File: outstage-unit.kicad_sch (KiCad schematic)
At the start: 10 parts, among them J2101 Conn_01x06_Socket, M2101 Fan

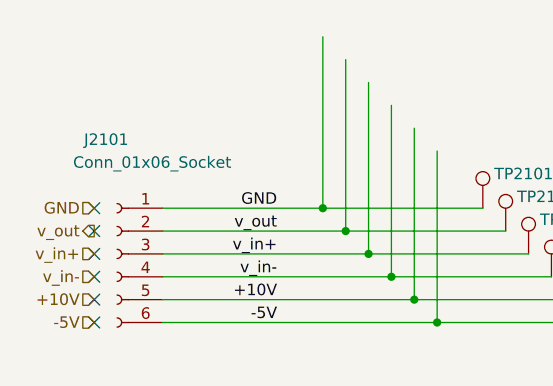
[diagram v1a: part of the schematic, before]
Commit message: edit outstage connector pin out for outstage-unit
enhance layout option with other pin out and mirror pinout for second outstage.
This allows to create a better layout with less crossing of high current tracks.
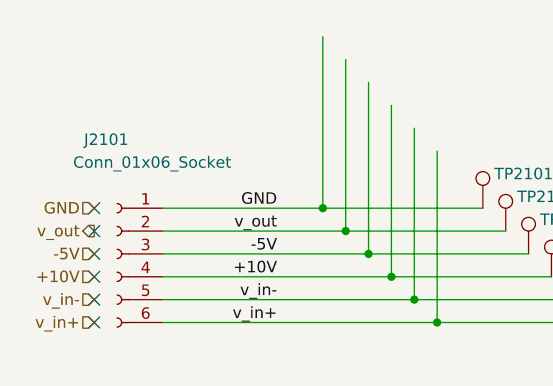
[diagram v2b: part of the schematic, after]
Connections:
- net +10V: now also J2101.4 (Pin_4), TP2104.1; no longer J2101.5 (Pin_5), TP2105.1
- net -5V: now also J2101.3 (Pin_3), TP2103.1; no longer J2101.6 (Pin_6), TP2106.1
- net v_in+: now also J2101.6 (Pin_6), TP2106.1; no longer J2101.3 (Pin_3), TP2103.1
- net v_in-: now also J2101.5 (Pin_5), TP2105.1; no longer J2101.4 (Pin_4), TP2104.1
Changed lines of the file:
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@@
 	(title_block
 		(title "Power Supply Sink")
-		(date "2024-12-07")
-		(rev "0.13.4")
+		(date "2024-12-08")
+		(rev "0.13.5")
 		(company "Open Battery Tester")
 		(comment 1 "Outstage Unit")
@@
 	)
 	(label "-5V"
-		(at 66.04 184.15 180)
+		(at 66.04 176.53 180)
 		(fields_autoplaced yes)
 		(effects
@@
 	)
 	(label "v_in+"
-		(at 66.04 176.53 180)
+		(at 66.04 184.15 180)
 		(fields_autoplaced yes)
 		(effects
@@
 	)
 	(label "+10V"
-		(at 66.04 181.61 180)
+		(at 66.04 179.07 180)
 		(fields_autoplaced yes)
 		(effects
@@
 	)
 	(label "v_in-"
-		(at 66.04 179.07 180)
+		(at 66.04 181.61 180)
 		(fields_autoplaced yes)
 		(effects
@@
 	(hierarchical_label "-5V"
 		(shape input)
-		(at 45.72 184.15 180)
+		(at 45.72 176.53 180)
 		(fields_autoplaced yes)
 		(effects
@@
 	(hierarchical_label "v_in+"
 		(shape input)
-		(at 45.72 176.53 180)
+		(at 45.72 184.15 180)
 		(fields_autoplaced yes)
 		(effects
@@
 	(hierarchical_label "+10V"
 		(shape input)
-		(at 45.72 181.61 180)
+		(at 45.72 179.07 180)
 		(fields_autoplaced yes)
 		(effects
@@
 	(hierarchical_label "v_in-"
 		(shape input)
-		(at 45.72 179.07 180)
+		(at 45.72 181.61 180)
 		(fields_autoplaced yes)
 		(effects
@@
 		(length 2.54)
 		(shape dot)
-		(at 78.74 160.02 0)
+		(at 83.82 165.1 0)
 		(fields_autoplaced yes)
 		(effects
@@
 		)
 		(property "Netclass" "3A"
-			(at 79.4385 157.48 0)
+			(at 84.5185 162.56 0)
 			(effects
 				(font
@@
 		(length 2.54)
 		(shape dot)
-		(at 76.2 157.48 0)
+		(at 81.28 162.56 0)
 		(fields_autoplaced yes)
 		(effects
@@
 		)
 		(property "Netclass" "3A"
-			(at 76.8985 154.94 0)
+			(at 81.9785 160.02 0)
 			(effects
 				(font
@@
 		(length 2.54)
 		(shape round)
-		(at 81.28 162.56 0)
+		(at 76.2 157.48 0)
 		(fields_autoplaced yes)
 		(effects
@@
 		)
 		(property "Netclass" "12A5"
-			(at 81.9785 160.02 0)
+			(at 76.8985 154.94 0)
 			(effects
 				(font
@@
 		(length 2.54)
 		(shape round)
-		(at 83.82 165.1 0)
+		(at 78.74 160.02 0)
 		(fields_autoplaced yes)
 		(effects
@@
 		)
 		(property "Netclass" "12A5"
-			(at 84.5185 162.56 0)
+			(at 79.4385 157.48 0)
 			(effects
 				(font

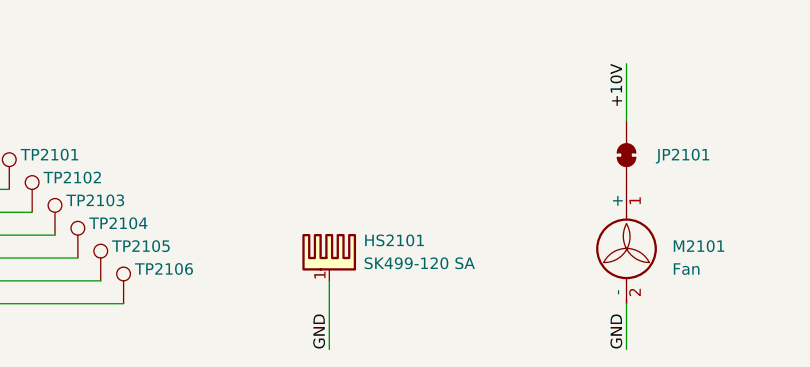
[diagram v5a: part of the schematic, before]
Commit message: fix outstage-unit symbol of heatsink, the heatsink is isolated
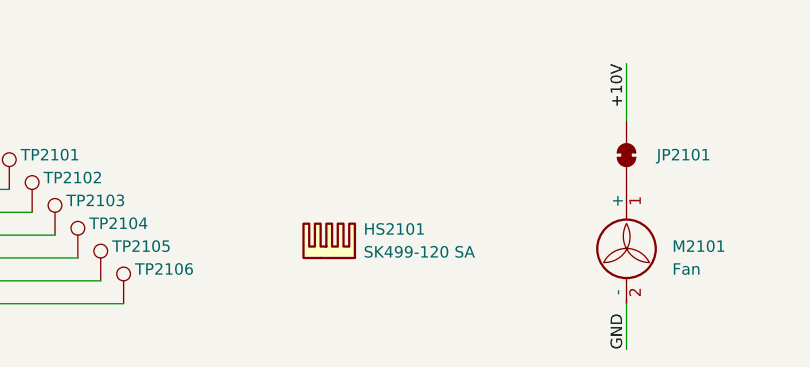
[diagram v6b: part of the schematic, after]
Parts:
- HS2101: symbol pss:Heatsink_Pad -> pss:Heatsink
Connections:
- net GND: no longer HS2101.1
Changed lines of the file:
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@@
 	(title_block
 		(title "Power Supply Sink")
-		(date "2024-12-09")
-		(rev "0.13.8")
+		(date "2024-12-10")
+		(rev "0.13.9")
 		(company "Open Battery Tester")
 		(comment 1 "Outstage Unit")
@@
 	(wire
 		(pts
-			(xy 124.46 189.23) (xy 124.46 181.61)
-		)
-		(stroke
-			(width 0)
-			(type default)
-		)
-	)
-	(wire
-		(pts
 			(xy 157.48 157.48) (xy 157.48 163.83)
 		)
@@
 			(width 0)
 			(type default)
-		)
-	)
-	(label "GND"
-		(at 124.46 189.23 90)
-		(fields_autoplaced yes)
-		(effects
-			(font
-				(size 1.27 1.27)
-			)
-			(justify left bottom)
 		)
 	)
@@
 	)
 	(symbol
-		(lib_id "pss:Heatsink_Pad")
+		(lib_id "pss:Heatsink")
 		(at 124.46 179.07 0)
 		(unit 1)
@@
 		(fields_autoplaced yes)
 		(property "Reference" "HS2101"
-			(at 128.27 177.1649 0)
+			(at 128.27 175.8949 0)
 			(effects
 				(font
@@
 		)
 		(property "Value" "SK499-120 SA"
-			(at 128.27 179.7049 0)
+			(at 128.27 178.4349 0)
 			(effects
 				(font
@@
 			)
 		)
-		(property "Description" "Heatsink with electrical connection, 1 pin"
+		(property "Description" "Heatsink"
 			(at 124.46 179.07 0)
 			(effects
@@
 			)
 		)
-		(pin "1"
-		)
 		(instances
